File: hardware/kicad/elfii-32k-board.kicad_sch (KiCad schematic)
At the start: 14 parts, among them J1 ELFII_P3_86, SW1 RAM_PAGE_ENABLE, U1 74HC573, U2 CY62256-70PC, U3 74LS151, U4 CD4011

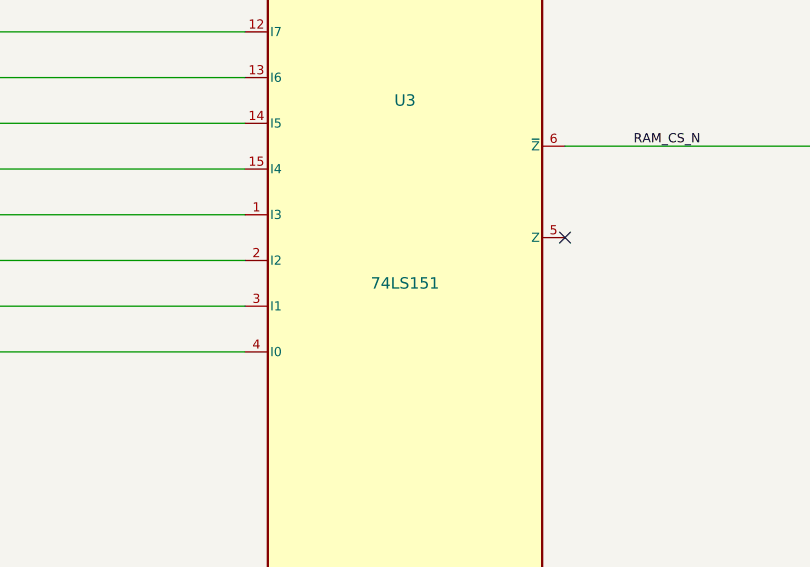
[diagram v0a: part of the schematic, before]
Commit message: Use pin-compatible 74HC151 to support 22k page-switch pull-downs
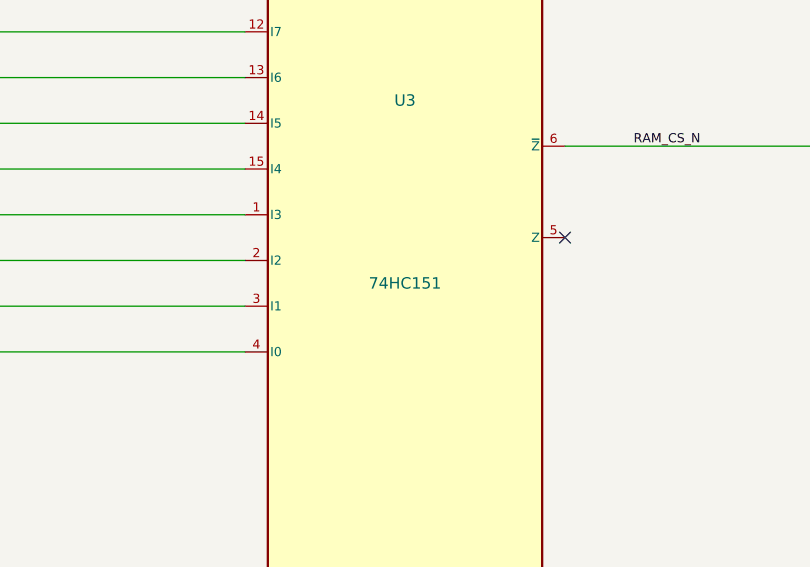
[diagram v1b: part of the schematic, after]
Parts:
- U3: value 74LS151 -> 74HC151; symbol ELFII_32K:74LS151 -> ELFII_32K:74HC151
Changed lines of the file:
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@@
 (generator "eeschema")
 (paper "A2")
-(title_block (title "Netronics ELF II 32K Static RAM Expansion") (date "2026-10-12") (rev "B5 - explicit write control") (company "Community restoration project") (comment 1 "Historical bus interface; NOT validated/fabrication-ready"))
+(title_block (title "Netronics ELF II 32K Static RAM Expansion") (date "2026-10-12") (rev "B6 - CMOS page mapper") (company "Community restoration project") (comment 1 "Historical bus interface; NOT validated/fabrication-ready"))
 (symbol (lib_id "ELFII_Expansion:ELFII_P3") (at 76.2 113.03 180) (unit 1) (in_bom no) (on_board yes) (dnp no)
 (property "Reference" "J1" (at 76.2 102.87 0) (effects (font (size 1.27 1.27))))
@@
 (instances (project "elfii-32k-board" (path "/89d8d6a8-e087-4cc0-b51a-852515026bd4" (reference "SW1") (unit 1))))
 )
-(symbol (lib_id "ELFII_32K:74LS151") (at 355.6 254 0) (unit 1) (in_bom yes) (on_board yes) (dnp no)
+(symbol (lib_id "ELFII_32K:74HC151") (at 355.6 254 0) (unit 1) (in_bom yes) (on_board yes) (dnp no)
 (property "Reference" "U3" (at 355.6 243.84 0) (effects (font (size 1.27 1.27))))
-(property "Value" "74LS151" (at 355.6 264.16 0) (effects (font (size 1.27 1.27))))
+(property "Value" "74HC151" (at 355.6 264.16 0) (effects (font (size 1.27 1.27))))
 (property "Footprint" "Package_DIP:DIP-16_W7.62mm" (at 355.6 254 0) (effects (font (size 1.27 1.27)) hide))
 (instances (project "elfii-32k-board" (path "/89d8d6a8-e087-4cc0-b51a-852515026bd4" (reference "U3") (unit 1))))

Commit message: Use correctly polarized through-hole radial footprint for 10uF C5 bulk capacitor
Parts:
- C5: footprint Capacitor_THT:C_Disc_D5.0mm_W2.5mm_P5.00mm -> Capacitor_THT:CP_Radial_D5.0mm_P2.00mm
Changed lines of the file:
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@@
 (generator "eeschema")
 (paper "A2")
-(title_block (title "Netronics ELF II 32K Static RAM Expansion") (date "2026-10-12") (rev "B6 - CMOS page mapper") (company "Community restoration project") (comment 1 "Historical bus interface; NOT validated/fabrication-ready"))
+(title_block (title "Netronics ELF II 32K Static RAM Expansion") (date "2026-10-12") (rev "B7 - electrical verified; PCB in progress") (company "Community restoration project") (comment 1 "Historical bus interface; NOT validated/fabrication-ready"))
 (symbol (lib_id "ELFII_Expansion:ELFII_P3") (at 76.2 113.03 180) (unit 1) (in_bom no) (on_board yes) (dnp no)
 (property "Reference" "J1" (at 76.2 102.87 0) (effects (font (size 1.27 1.27))))
@@
 (property "Reference" "C5" (at 469.9 147.32000000000002 0) (effects (font (size 1.27 1.27))))
 (property "Value" "10u" (at 469.9 167.64000000000001 0) (effects (font (size 1.27 1.27))))
-(property "Footprint" "Capacitor_THT:C_Disc_D5.0mm_W2.5mm_P5.00mm" (at 469.9 157.48000000000002 0) (effects (font (size 1.27 1.27)) hide))
+(property "Footprint" "Capacitor_THT:CP_Radial_D5.0mm_P2.00mm" (at 469.9 157.48000000000002 0) (effects (font (size 1.27 1.27)) hide))
 (instances (project "elfii-32k-board" (path "/89d8d6a8-e087-4cc0-b51a-852515026bd4" (reference "C5") (unit 1))))
 )
